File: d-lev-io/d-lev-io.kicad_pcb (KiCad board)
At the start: 4 copper layers, 148.4 x 50.1 mm, 144 parts, among them IC1 ES9010K2M, IC3 MAX97220C/MAX97220D, J1 USB_C_Receptacle_USB2.0, J2 PJ-059A, J3 Conn_01x12_MountingPin, J4 MIDI_OUT_JACK, J5 PROG_HDR, J6 HEADPHONE, SW1 SW_Push, SW2 SW_Push, SW3 SW_Push, U1 ATSAMD11D14A-M, U2 TPS54202DDC, U3 ADP151-3.3, U4 74LVC2GU04, U5 AP2112K-3.3, U6 74AHC1G126, X1 7M-50.000MAAJ-T

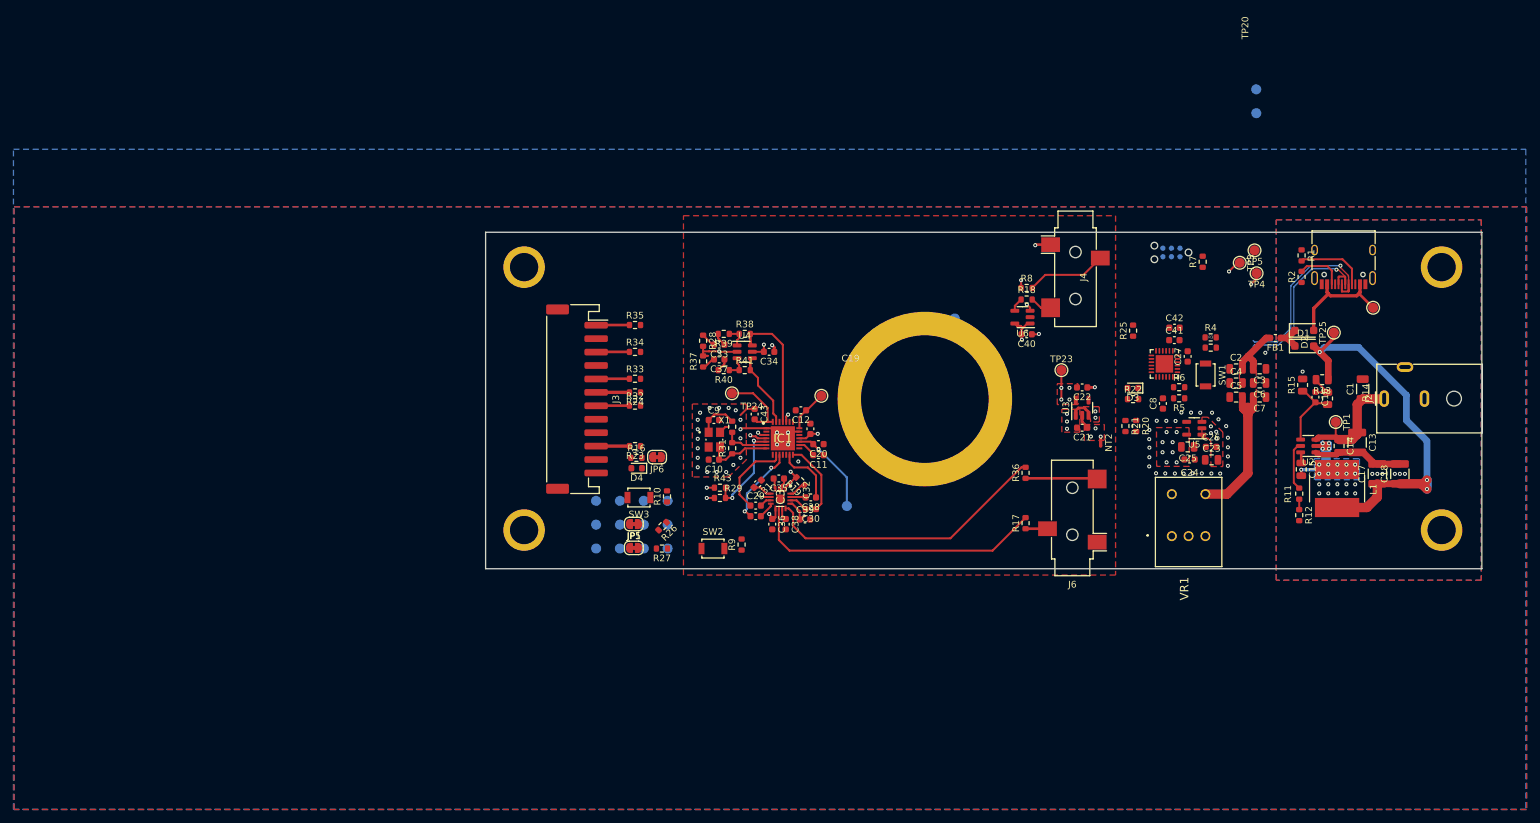
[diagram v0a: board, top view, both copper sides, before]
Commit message: Routed IO board
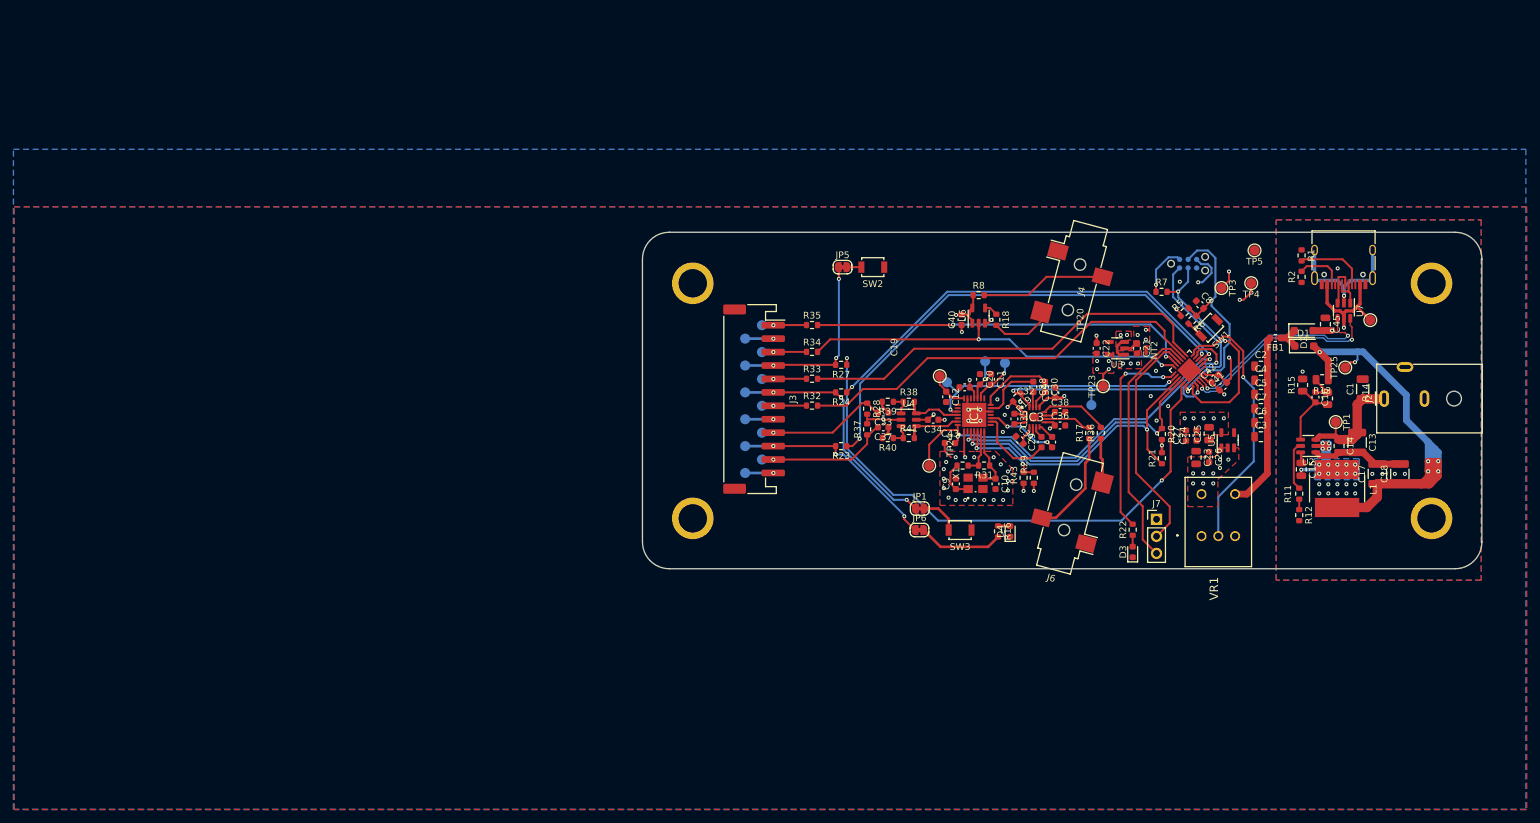
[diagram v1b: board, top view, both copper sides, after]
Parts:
- removed H3: MountingHole_Pad, theremin:MicStandHole
- removed R10: 4.7k, Resistor_SMD:R_0603_1608Metric
- removed R25, R26: 0, Resistor_SMD:R_0603_1608Metric
- removed R3, R4: 22, Resistor_SMD:R_0603_1608Metric
- removed R9: 2.2k, Resistor_SMD:R_0603_1608Metric
- added C45: 0.1u, Capacitor_SMD:C_0805_2012Metric, F.Cu at (219.7, 65.5)
- added J7: TOUCH_HDR, Connector_PinHeader_2.54mm:PinHeader_1x03_P2.54mm_Vertical, F.Cu at (194.5, 94.6)
- added U7: USBLC6-2SC6, Package_TO_SOT_SMD:SOT-23-6, F.Cu at (222.4, 63.5)
- R7: value 10k -> 1k
- moved TP19 63.4 mm to (163.3, 74.2)
- moved D4 56.4 mm to (172.7, 96.4), turned to 90 degrees
- moved R16 54.9 mm to (170.9, 96.4), turned to -90 degrees
- moved JP5 52.1 mm to (147.8, 57.0)
- moved TP20 49.9 mm to (184.8, 77.6)
- moved SW2 48.2 mm to (152.2, 57.0), turned to 180 degrees
- moved SW3 48.1 mm to (165.2, 96.2)
- moved R29 46.8 mm to (176.2, 88.4), turned to 90 degrees
- moved C32 45.5 mm to (178.9, 83.1), turned to 90 degrees
- moved C36 45.3 mm to (180.1, 80.6), turned to 0 degrees
- moved R43 45.2 mm to (174.7, 88.4), turned to 90 degrees
- moved C38 44.1 mm to (180.1, 78.6), turned to 0 degrees
- moved C29 43.6 mm to (177.4, 83.1), turned to 90 degrees
- moved JP1 42.6 mm to (159.2, 93.0), turned to 0 degrees
- moved C10 42.1 mm to (170.5, 89.3), turned to -90 degrees
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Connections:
- C11 pad 1: GNDA -> GND
- C12 pad 2: GNDA -> GND
- C19 pad 1: GNDA -> GND
- C20 pad 1: GNDA -> GND
- C31 pad 1: GNDA -> GND
- C36 pad 2: GNDA -> GND
- C38 pad 2: GNDA -> GND
- C39 pad 2: GNDA -> GND
- IC1 pad 12: GNDA -> GND
- IC3 pad 3: GNDA -> GND
- IC3 pad 6: GNDA -> GND
- J6 pad S: GNDA -> GND
- NT2 pad 2: GNDA -> GND
- U1 pad 10: Net-(U1-PA11) -> /SAMD11/PTC_X3Y9
- U1 pad 9: Net-(U1-PA10) -> /SAMD11/PTC_X2Y8
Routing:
- net Net-(U1-PA27): track 0.00 -> 84.1 mm, vias 0 -> 2
- net Net-(U1-PA05): track 0.00 -> 72.0 mm, vias 0 -> 2
- net Net-(U1-PA04): track 0.00 -> 65.9 mm, vias 0 -> 2
- net uart_tx_3v: track 0.00 -> 63.0 mm
- net uart_rx_3v: track 0.00 -> 62.5 mm
- net midi_from_fpga_3v: track 0.00 -> 58.0 mm, vias 0 -> 2
- net midi_to_fpga_3v: track 0.00 -> 57.4 mm, vias 0 -> 2
- net /DAC/DAC_RESET: track 11.2 -> 62.5 mm, vias 0 -> 2
- net /DAC/SDA: track 2.58 -> 47.4 mm, vias 1 -> 2
- net /DAC/SCL: track 1.38 -> 43.5 mm, vias 1 -> 2
- net /SAMD11/VOLUME_POT: track 0.00 -> 40.2 mm, vias 0 -> 1
- net /DAC/DAC_GPIO: track 1.20 -> 40.1 mm, vias 1 -> 2
- net /SAMD11/PTC_X2Y8: track 0.00 -> 37.7 mm
- net /DAC/OUT_SE_R: track 44.1 -> 7.22 mm
- net /DAC/HPA_SHDN: track 2.59 -> 38.9 mm, vias 0 -> 2
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- added copper zone on In2.Cu, net VDD
- removed copper zone on F.Cu, net GNDA
- removed copper zone on F.Cu, net SWITCH_LOW
- removed copper zone on B.Cu, net VDD
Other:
- board size 148.4 x 50.1 mm -> 125 x 50.1 mm
- board text added: "https://www.digikey.com/en/maker/projects/how-to-route-differential-pairs-in-kicad-for-usb/45b99011f5d34879ae1831dce1f13e93"

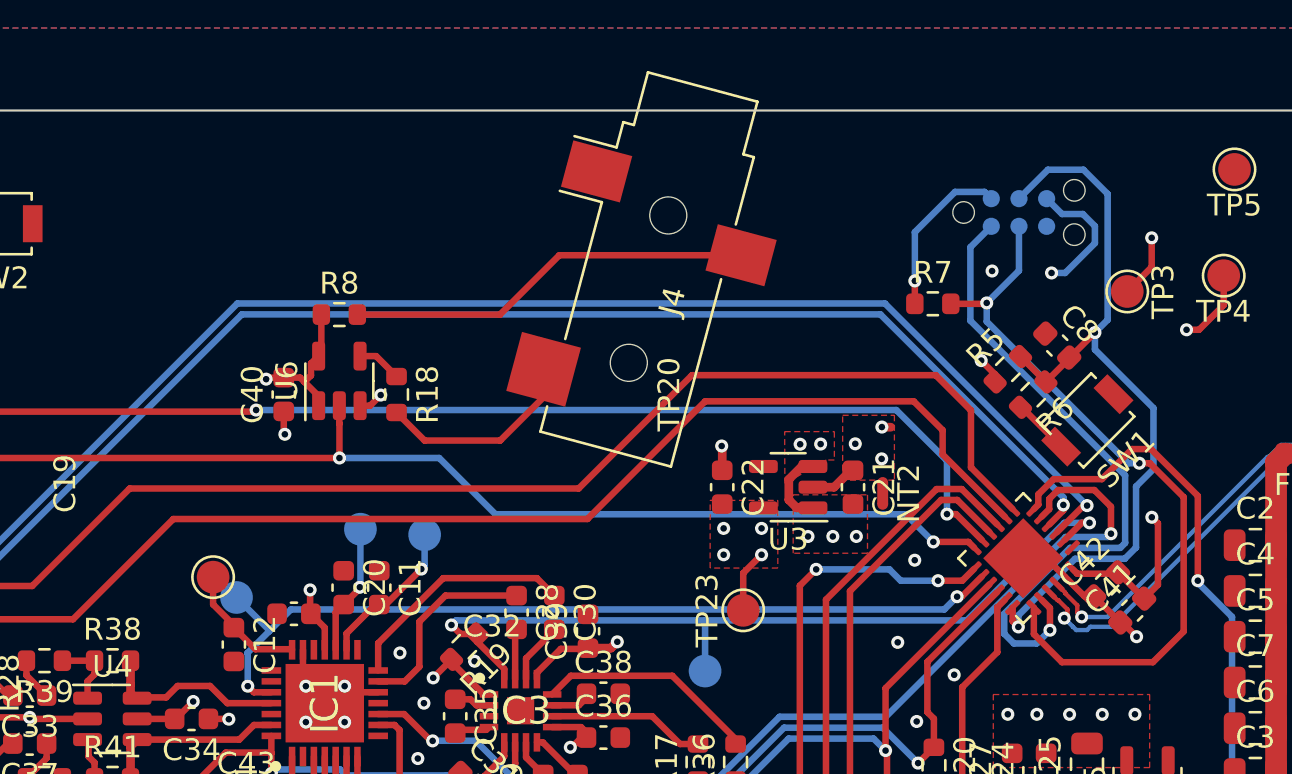
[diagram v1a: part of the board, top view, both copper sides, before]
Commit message: add 5-pin CV expansion header
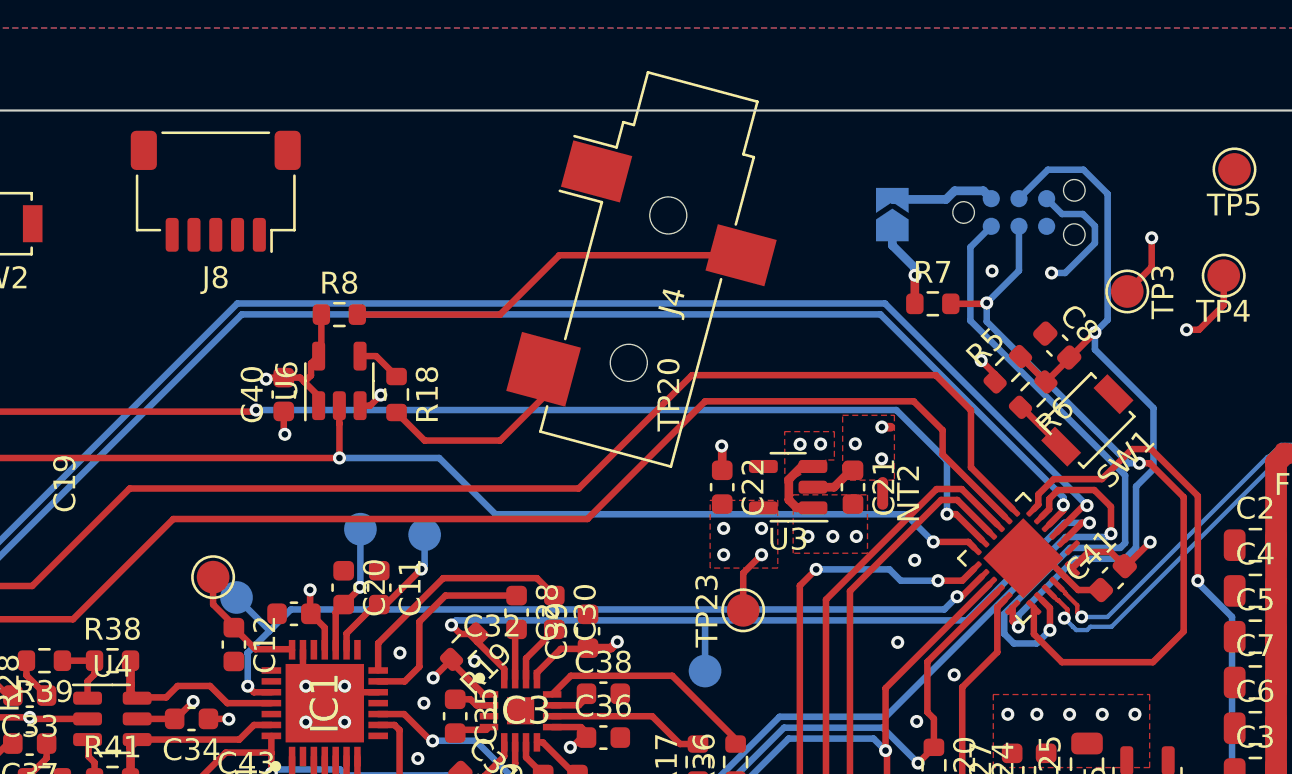
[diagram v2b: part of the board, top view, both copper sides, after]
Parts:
- removed C42: .1u, Capacitor_SMD:C_0603_1608Metric
- added J8: CV_HDR, Connector_JST:JST_SH_SM05B-SRSS-TB_1x05-1MP_P1.00mm_Horizontal, F.Cu at (162.3, 55.6)
- added JP2: PROG_VIN, theremin:SolderJumper-2_P1.3mm_Open_TrianglePad1.0x1.5mm, B.Cu at (193.4, 56.6)
- C41: value 10u -> 4.7u
- moved C41 1.74 mm to (203.5, 73.3)
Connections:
- J5 pad 1: +3V3 -> Net-(J5-Pin_1)
- U1 pad 1: /SAMD11/DAC_INTERNAL -> /SAMD11/CV_EN
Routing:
- net +3V3: track 37.2 -> 29.9 mm
- net Net-(J5-Pin_1): track 0.00 -> 4.86 mm
- net GND: track 86.3 -> 83.8 mm, vias 62 -> 61

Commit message: route cv header
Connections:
- J8 pad 3: /DAC/SDA -> /DAC/SCL
- J8 pad 4: /DAC/SCL -> /DAC/SDA
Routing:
- net /SAMD11/CV_EN: track 0.00 -> 50.6 mm, vias 0 -> 2
- net /DAC/SDA: track 47.4 -> 78.5 mm, vias 2 -> 3
- net /DAC/SCL: track 43.5 -> 73.7 mm, vias 2 -> 3
- net /SAMD11/JTAG.SWCLK: track 34.4 -> 32.4 mm
- net VDD: track 17.3 -> 18.9 mm, vias 17 -> 18
- net /SAMD11/JTAG.SWDIO: track 29.8 -> 29.0 mm
- net Net-(U1-PA05): track 72.0 -> 72.6 mm
- net Net-(U1-PA04): track 65.9 -> 66.6 mm
- net /DAC/DAC_RESET: track 62.5 -> 62.0 mm
- net /SAMD11/~{RST}: track 36.1 -> 35.6 mm
- net GND: vias 61 -> 62

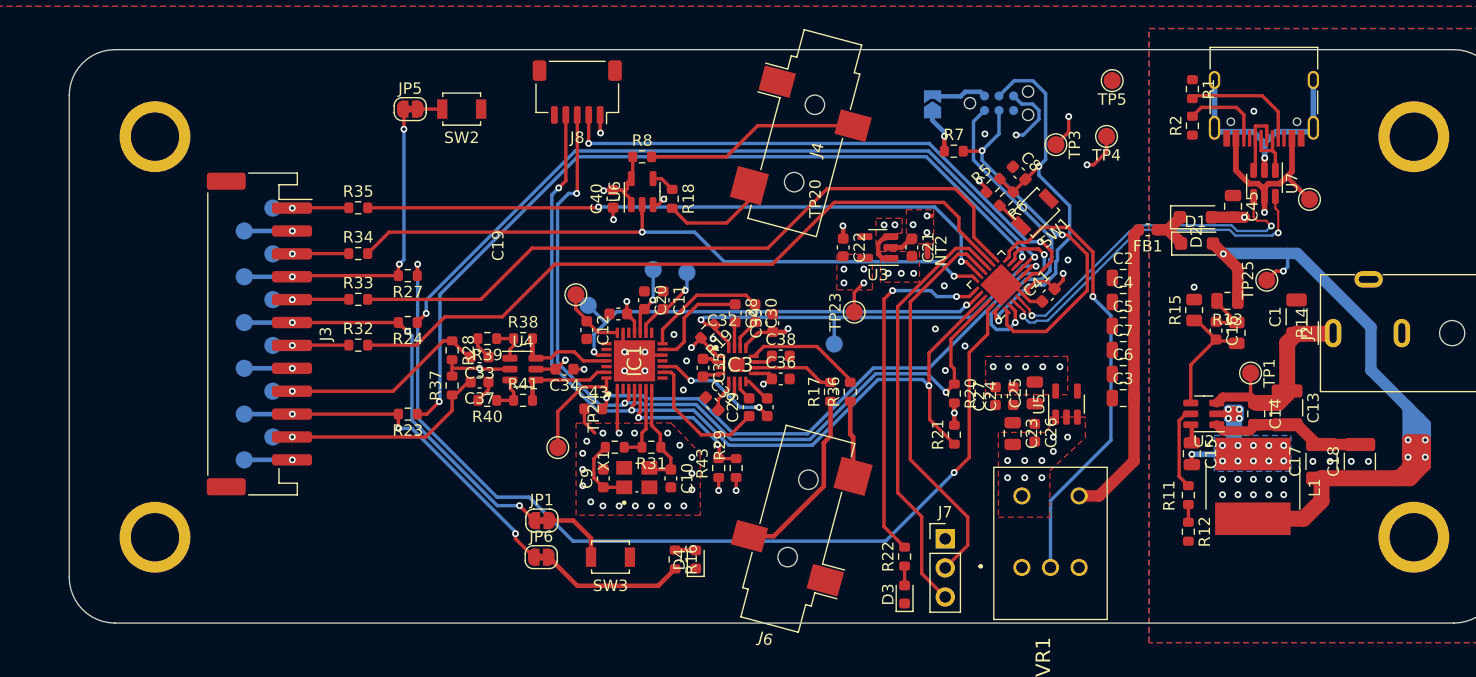
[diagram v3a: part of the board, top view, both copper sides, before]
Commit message: I/O board silk placement
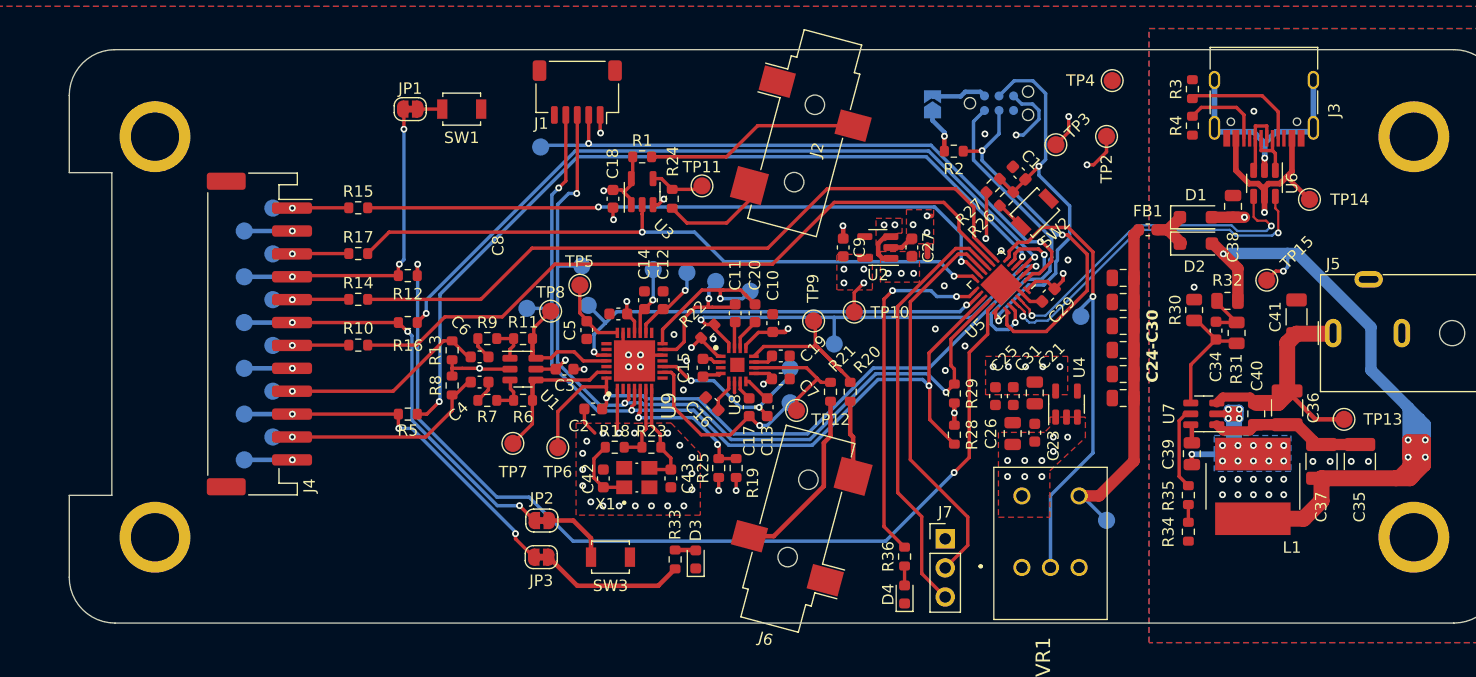
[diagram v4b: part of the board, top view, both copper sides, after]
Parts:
- added TP1: TestPoint, TestPoint:TestPoint_Pad_D1.5mm, B.Cu at (159.1, 60.4)
- added TP11: VUSB, TestPoint:TestPoint_Pad_D1.5mm, F.Cu at (173.2, 63.8)
- added TP12: SE_R, TestPoint:TestPoint_Pad_D1.5mm, F.Cu at (181.5, 83.4)
- added TP16: TestPoint, TestPoint:TestPoint_Pad_D1.5mm, B.Cu at (206.3, 75.2)
- added TP17: BAL_R-, TestPoint:TestPoint_Pad_D1.5mm, B.Cu at (180.9, 79.7)
- added TP18: BAL_R+, TestPoint:TestPoint_Pad_D1.5mm, B.Cu at (180.9, 82.7)
- added TP19: BAL_L+, TestPoint:TestPoint_Pad_D1.5mm, B.Cu at (174.4, 72.1)
- added TP20: BAL_L-, TestPoint:TestPoint_Pad_D1.5mm, B.Cu at (177.4, 73.0)
- added TP24: TestPoint, TestPoint:TestPoint_Pad_D1.5mm, B.Cu at (157.9, 74.5)
- added TP25: TestPoint, TestPoint:TestPoint_Pad_D1.5mm, B.Cu at (162.7, 70.8)
- added TP39: VDD_B4SW, TestPoint:TestPoint_Pad_D1.5mm, B.Cu at (208.6, 93.0)
- added TP7: VUSB, TestPoint:TestPoint_Pad_D1.5mm, F.Cu at (156.7, 86.3)
- added TP8: VUSB, TestPoint:TestPoint_Pad_D1.5mm, F.Cu at (160.0, 74.7)
- added TP9: SE_L, TestPoint:TestPoint_Pad_D1.5mm, F.Cu at (183.0, 75.6)
- moved TP13 9.11 mm to (229.3, 84.2)
- moved TP5 0.90 mm to (162.6, 72.4)
- moved D2 0.09 mm to (216.4, 68.8)
- renumbered C8 to C1, C39 to C10, C28 to C11, C11 to C12, C32 to C13, C20 to C14, C35 to C15, C31 to C16, C29 to C17, C40 to C18, C38 to C19, C43 to C2, C30 to C20, C27 to C21, C5 to C22, C26 to C23, C3 to C24, C23 to C26, C21 to C27, C6 to C28, C41 to C29, C34 to C3, C2 to C30, C24 to C31, C7 to C32, C4 to C33, C16 to C34, C18 to C35, C13 to C36, C17 to C37, C45 to C38, C15 to C39, C37 to C4, C14 to C40, C1 to C41, C9 to C42, C10 to C43, C12 to C5, C33 to C6, C36 to C7, C19 to C8, C22 to C9, D2 to D1, D1 to D2, D4 to D3, D3 to D4, H4 to H1, H5 to H3, H1 to H4, J8 to J1, J4 to J2, J1 to J3, J3 to J4, J2 to J5, J5 to J8, JP5 to JP1, JP1 to JP2, JP6 to JP3, JP2 to JP4, NT2 to NT1, R8 to R1, R32 to R10, R38 to R11, R27 to R12, R28 to R13, R33 to R14, R35 to R15, R24 to R16, R34 to R17, R30 to R18, R29 to R19, R7 to R2, R36 to R20, R17 to R21, R19 to R22, R31 to R23, R18 to R24, R43 to R25, R6 to R26, R5 to R27, R21 to R28, R20 to R29, R1 to R3, R15 to R30, R14 to R31, R13 to R32, R16 to R33, R12 to R34, R11 to R35, R22 to R36, R2 to R4, R23 to R5, R41 to R6, R40 to R7, R37 to R8, R39 to R9, SW2 to SW1, SW1 to SW2, TP23 to TP10, TP1 to TP13, TP2 to TP14, TP25 to TP15, TP4 to TP2, TP20 to TP21, TP21 to TP22, TP22 to TP23, TP19 to TP26, TP9 to TP27, TP15 to TP28, TP8 to TP29, TP12 to TP30, TP13 to TP31, TP6 to TP32, TP7 to TP33, TP14 to TP34, TP16 to TP35, TP10 to TP36, TP17 to TP37, TP11 to TP38, TP5 to TP4, TP24 to TP5, TP18 to TP6, U4 to U1, U3 to U2, U6 to U3, U5 to U4, U1 to U5, U7 to U6, U2 to U7, IC3 to U8, IC1 to U9
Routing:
- net /DAC/OUT_SE_L: track 10.2 -> 15.6 mm
- net /DAC/OUT_BAL.R+: track 12.2 -> 16.9 mm, vias 0 -> 1
- net /DAC/OUT_BAL.R-: track 11.0 -> 15.5 mm
- net /DAC/SPDIF2: track 8.34 -> 12.8 mm
- net /SAMD11/CV_EN: track 50.6 -> 54.9 mm
- net /DAC/OUT_BAL.L-: track 10.9 -> 14.9 mm, vias 0 -> 1
- net +12V: track 18.1 -> 21.9 mm
- net /DAC/OUT_SE_R: track 7.22 -> 10.8 mm
- net SWITCH_LOW: track 26.4 -> 29.7 mm
- net /DAC/SPDIF1: track 10.3 -> 13.5 mm
- net +3V3: track 30.0 -> 32.8 mm
- net Net-(R24-Pad1): track 2.06 -> 4.79 mm
- net /DAC/OUT_BAL.L+: track 9.19 -> 11.7 mm, vias 0 -> 1
- net /DAC/SDA: track 78.5 -> 80.9 mm
- net /DAC/SCL: track 73.7 -> 75.8 mm
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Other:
- outline, holes or cut-outs redrawn
- board text added: "C24-C30"
